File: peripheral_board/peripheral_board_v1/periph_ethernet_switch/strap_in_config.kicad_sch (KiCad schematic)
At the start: 21 parts, among them J10 Conn_01x03, J11 Conn_01x03, J12 Conn_01x03, J6 Conn_01x03, J7 Conn_01x03, J8 Conn_01x03, J9 Conn_01x03

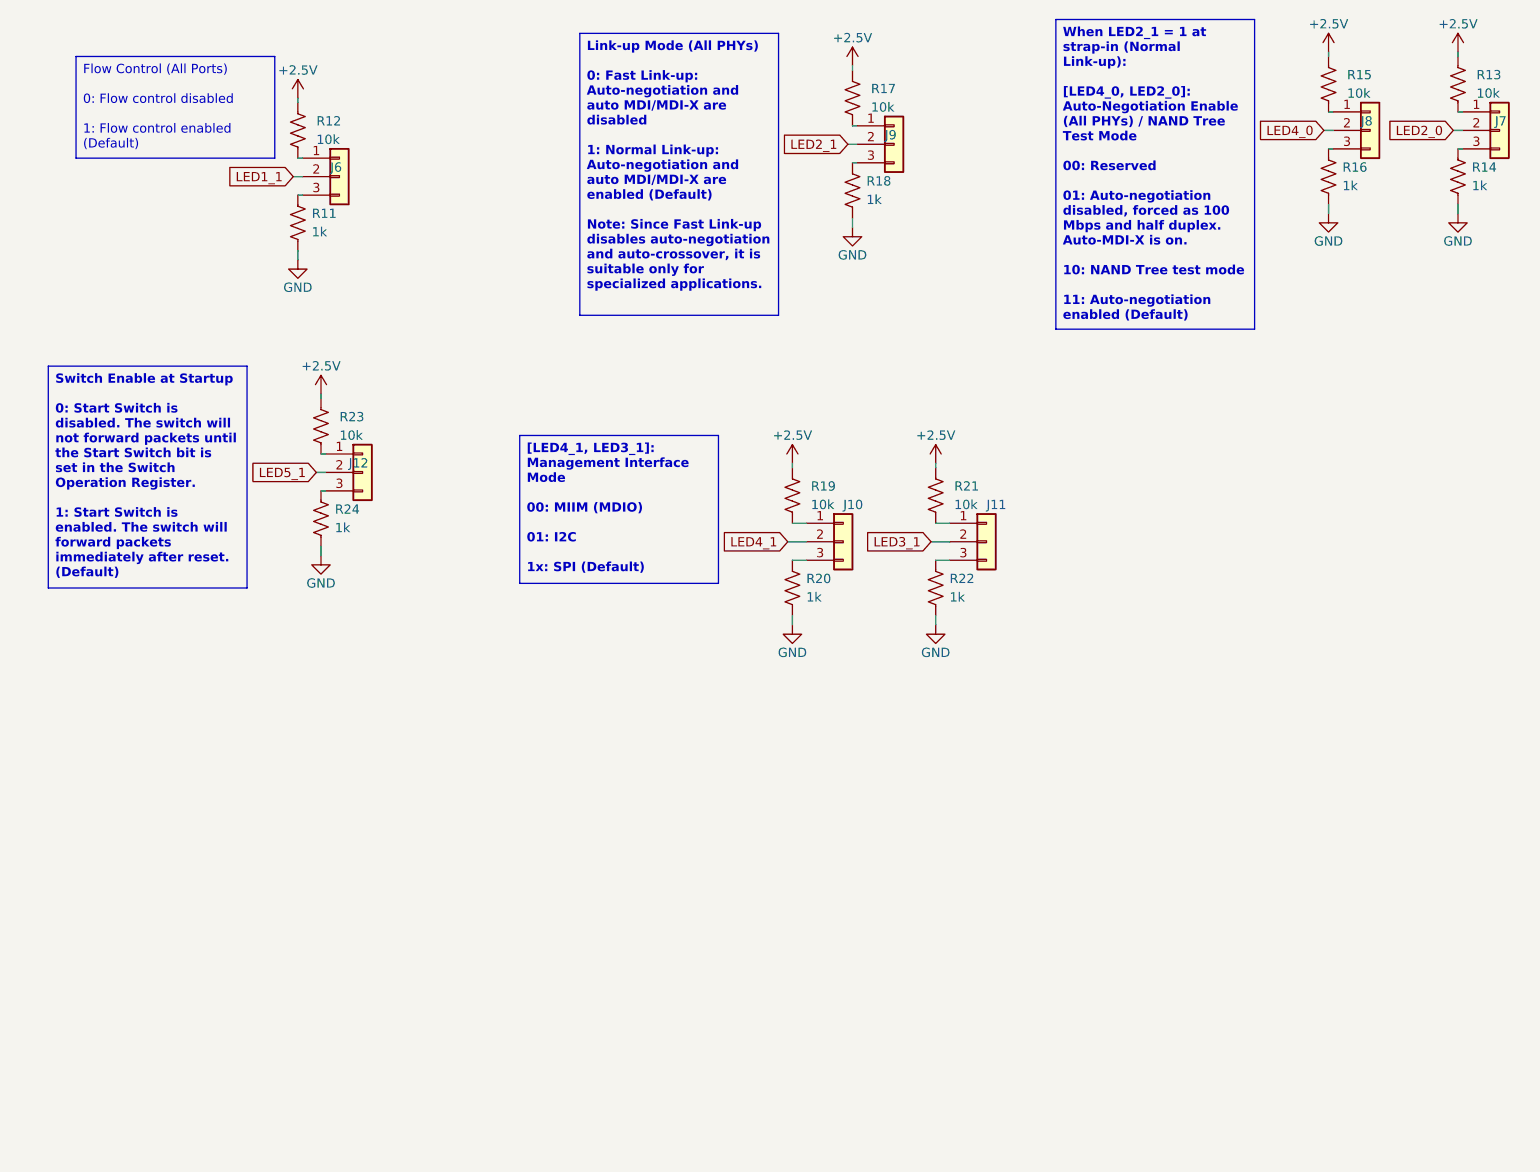
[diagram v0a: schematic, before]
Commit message: Switch Schematic Update
The switch schematic should be done. Waiting on a review but should be ready for moving forward with board layout.
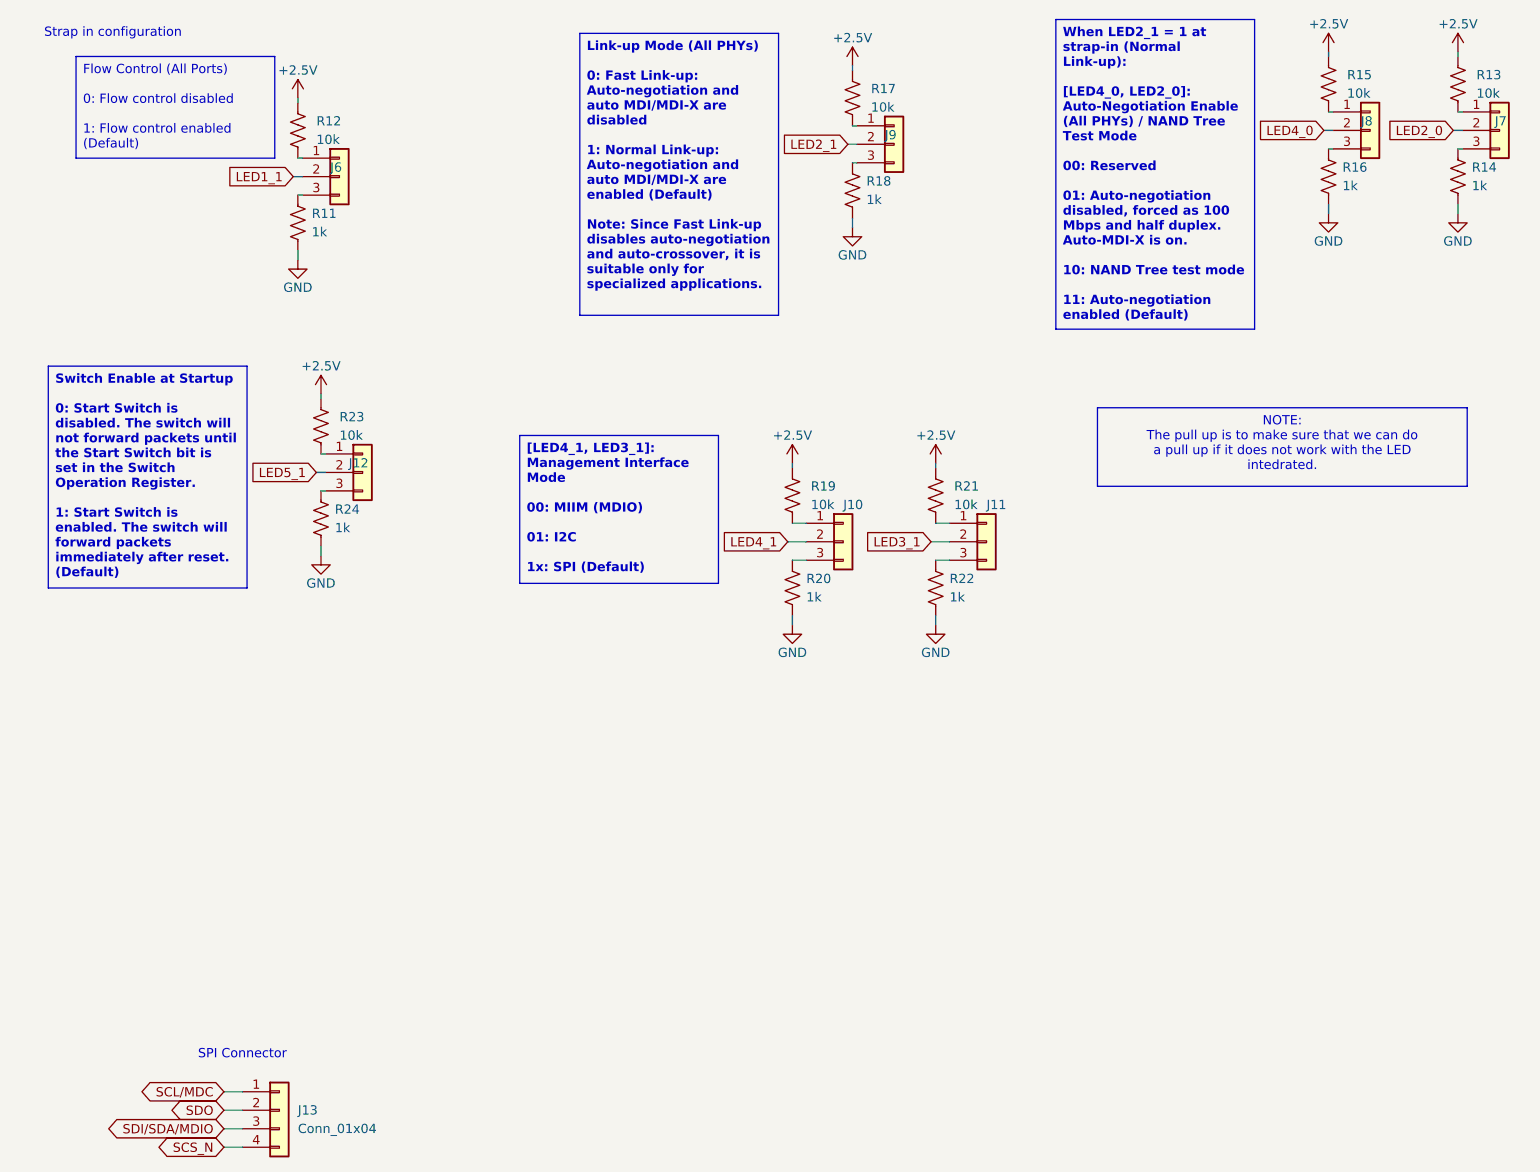
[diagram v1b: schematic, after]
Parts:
- added J13: Conn_01x04, Connector_PinHeader_2.54mm:PinHeader_1x04_P2.54mm_Vertical, symbol Connector_Generic:Conn_01x04
- R11, R12, R13, R14, R15, R16, R17, R18, R19, R20, R21, R22, R23, R24: footprint (none) -> Resistor_SMD:R_0603_1608Metric
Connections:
- new net SCL/MDC: J13.1 (Pin_1)
- new net SCS_N: J13.4 (Pin_4)
- new net SDI/SDA/MDIO: J13.3 (Pin_3)
- new net SDO: J13.2 (Pin_2)
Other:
- note added: "SPI Connector"
- note added: "Strap in configuration"

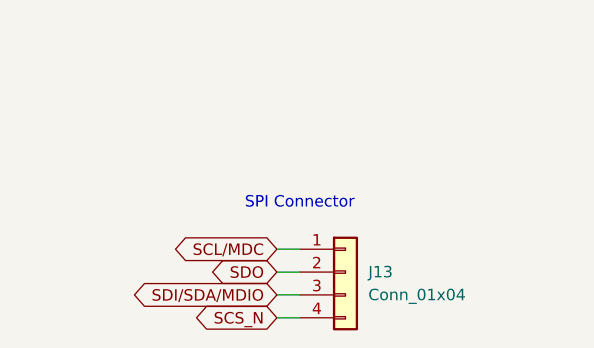
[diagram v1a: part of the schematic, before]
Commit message: Switch PCB layout done
The layout should be done. there are a lot of DRC errors but it seems like it is all for things like through holes and other similar items are causing this.
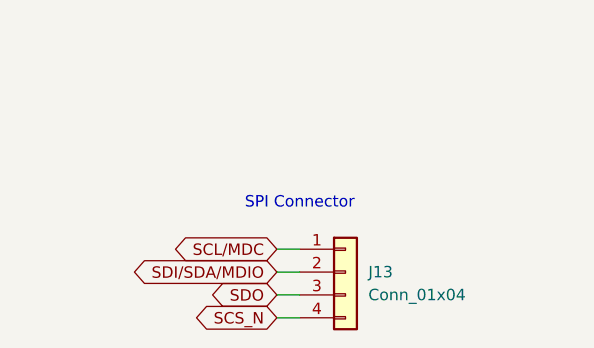
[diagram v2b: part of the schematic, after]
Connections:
- net SDI/SDA/MDIO: now also J13.2 (Pin_2); no longer J13.3 (Pin_3)
- net SDO: now also J13.3 (Pin_3); no longer J13.2 (Pin_2)
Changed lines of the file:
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@@
+	(wire
+		(pts
+			(xy 40.64 166.37) (xy 43.18 166.37)
+		)
+		(stroke
+			(width 0)
+			(type default)
+		)
+	)
 	(wire
 		(pts
@@
 	(wire
 		(pts
+			(xy 40.64 163.83) (xy 43.18 163.83)
+		)
+		(stroke
+			(width 0)
+			(type default)
+		)
+	)
+	(wire
+		(pts
 			(xy 53.34 76.2) (xy 54.61 76.2)
 		)
@@
 	(wire
 		(pts
-			(xy 40.64 166.37) (xy 43.18 166.37)
-		)
-		(stroke
-			(width 0)
-			(type default)
-		)
-	)
-	(wire
-		(pts
 			(xy 210.185 18.415) (xy 210.185 19.05)
 		)
@@
 		(pts
 			(xy 192.405 39.37) (xy 192.405 40.64)
-		)
-		(stroke
-			(width 0)
-			(type default)
-		)
-	)
-	(wire
-		(pts
-			(xy 40.64 163.83) (xy 43.18 163.83)
 		)
 		(stroke
@@
 	(global_label "SDI{slash}SDA{slash}MDIO"
 		(shape bidirectional)
-		(at 40.64 166.37 180)
+		(at 40.64 163.83 180)
 		(fields_autoplaced yes)
 		(effects
@@
 		)
 		(property "Intersheetrefs" "${INTERSHEET_REFS}"
-			(at 22.5734 166.37 0)
+			(at 22.5734 163.83 0)
 			(effects
 				(font
@@
 	(global_label "SDO"
 		(shape bidirectional)
-		(at 40.64 163.83 180)
+		(at 40.64 166.37 180)
 		(fields_autoplaced yes)
 		(effects
@@
 		)
 		(property "Intersheetrefs" "${INTERSHEET_REFS}"
-			(at 32.7335 163.83 0)
+			(at 32.7335 166.37 0)
 			(effects
 				(font

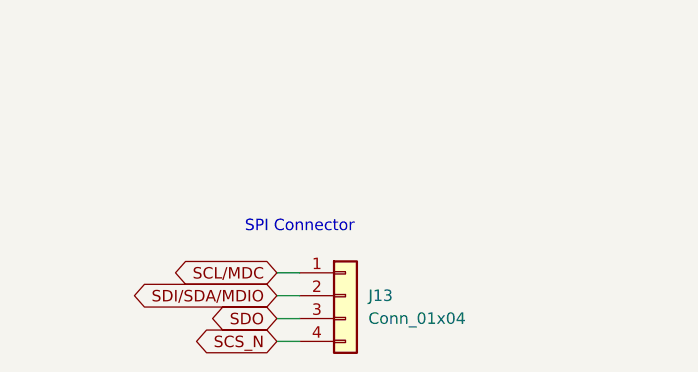
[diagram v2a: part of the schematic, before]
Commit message: WIP for new switch
Made some minor changes which are detailed in Notion.
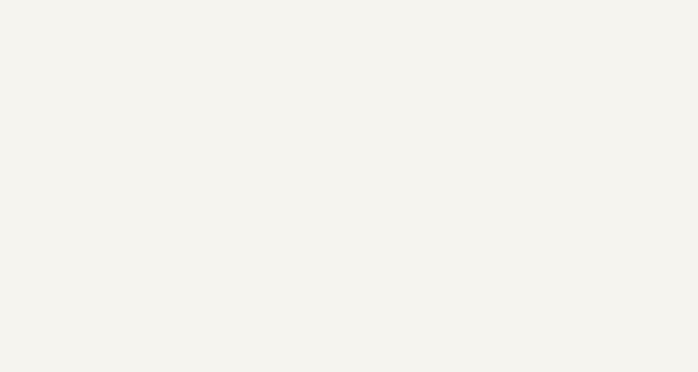
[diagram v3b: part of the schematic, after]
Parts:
- removed J13: Conn_01x04, Connector_PinHeader_2.54mm:PinHeader_1x04_P2.54mm_Vertical, symbol Connector_Generic:Conn_01x04
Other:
- note removed: "SPI Connector"

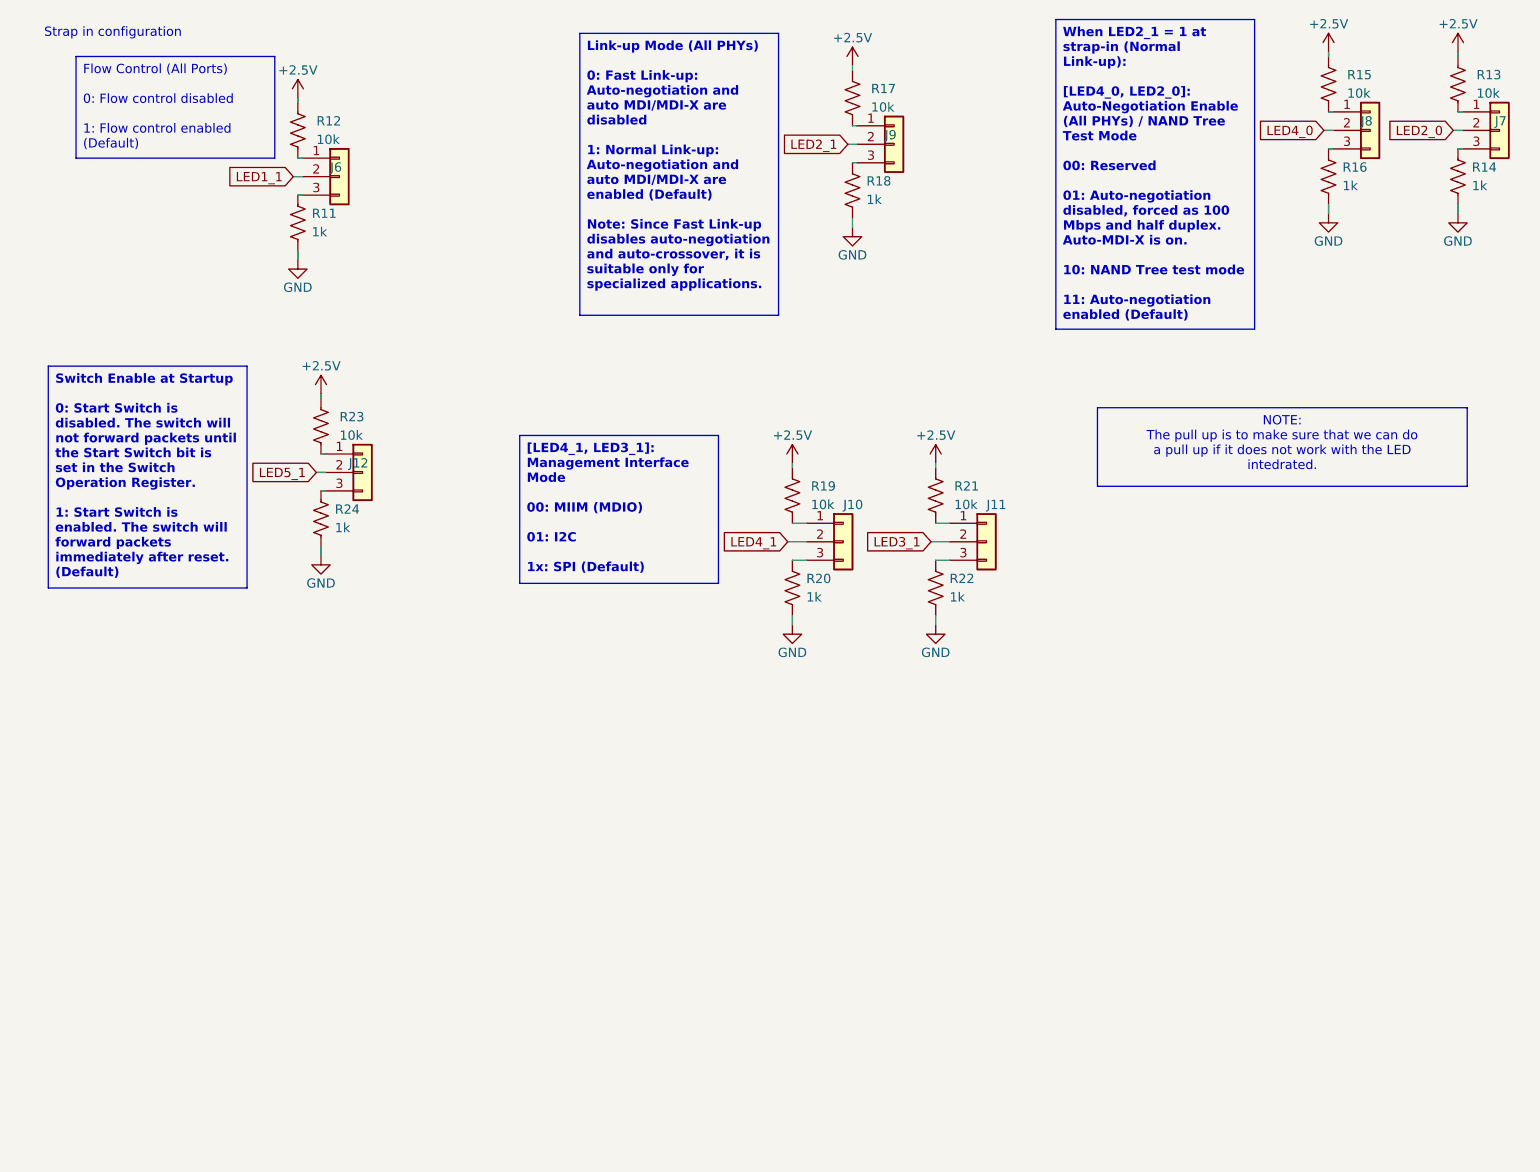
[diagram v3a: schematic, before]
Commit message: Changes to the board layout
Need to finish doing some layout but waiting on Microchip to confirm with what I have. Might want to change the EDA symbol for the switch IC.
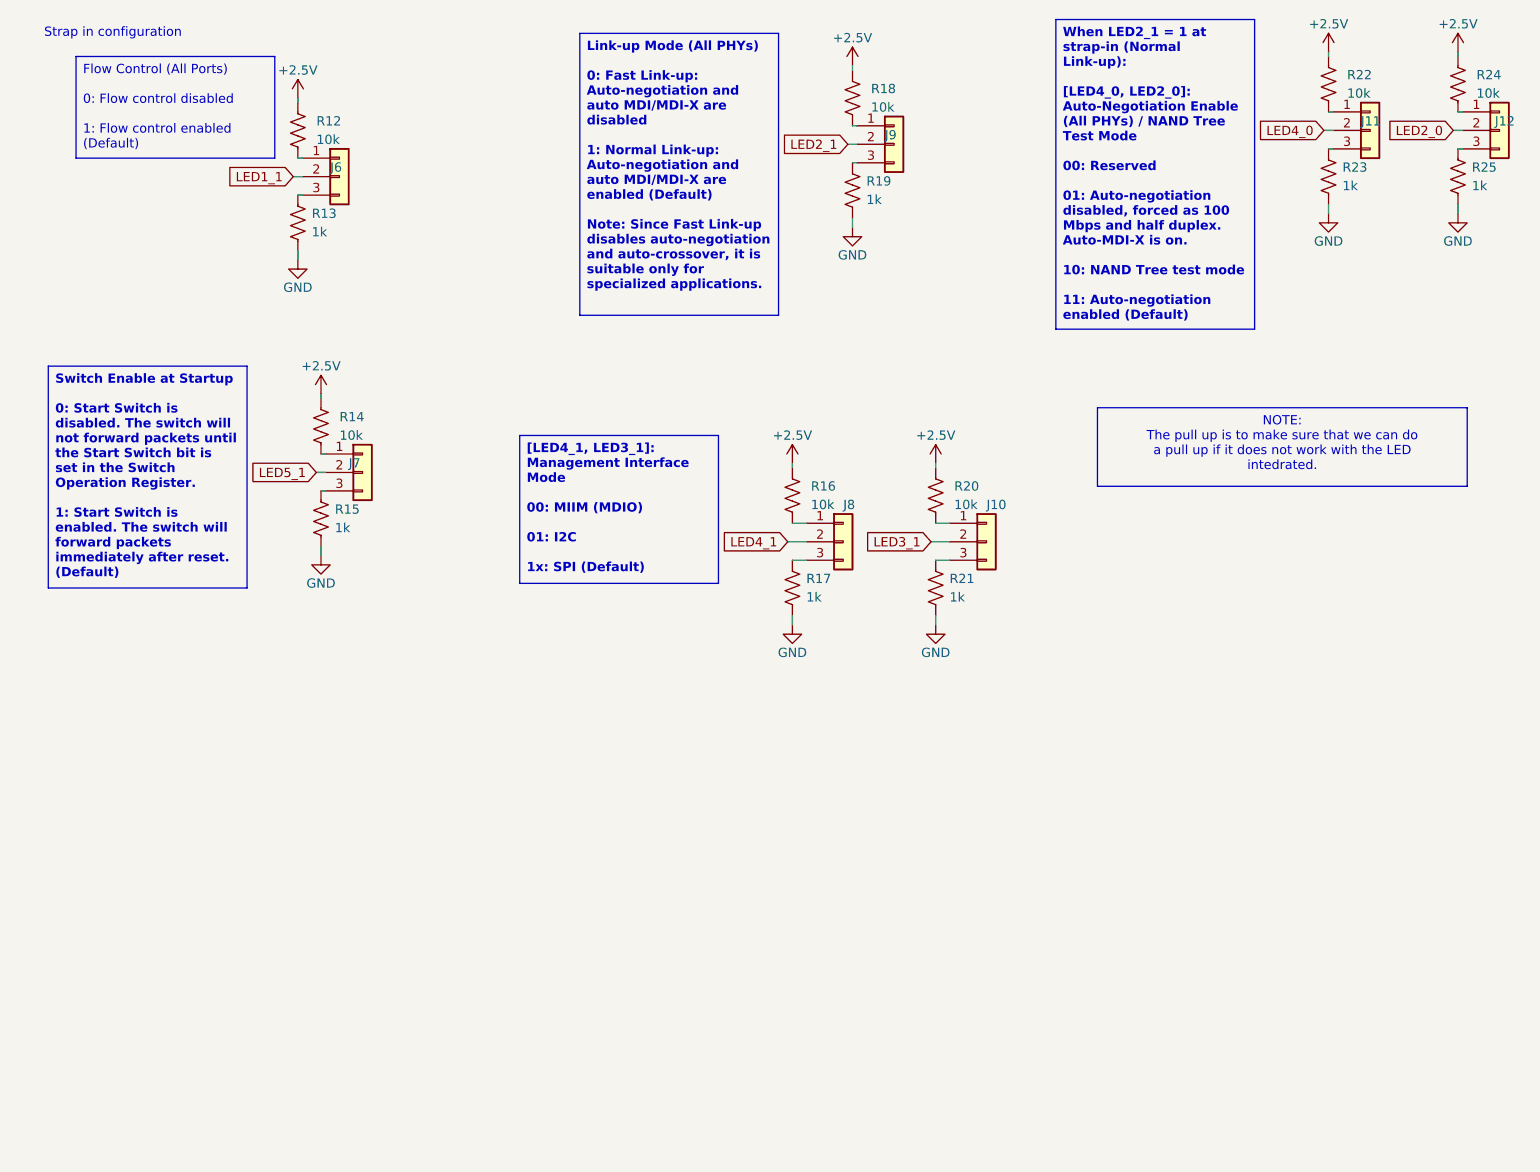
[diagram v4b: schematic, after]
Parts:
- renumbered J11 to J10, J8 to J11, J7 to J12, J12 to J7, J10 to J8, R11 to R13, R23 to R14, R24 to R15, R19 to R16, R20 to R17, R17 to R18, R18 to R19, R21 to R20, R22 to R21, R15 to R22, R16 to R23, R13 to R24, R14 to R25
